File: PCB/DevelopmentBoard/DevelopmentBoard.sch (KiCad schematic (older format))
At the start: 21 parts, among them U1 Pi_CM4, U2 Barometer_Grove, U3 D24V22F5, U4 Micro-USB, U5 VN-100_Breakout, X1 XT30-F_Connector, X2 XT30-F_Connector, X3 2mmGrove_Connector

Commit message: Moved Altimeter and RF module for better I2C routing
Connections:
- wire segments 32 -> 33
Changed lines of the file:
@@
 Wire Wire Line
 	5700 6100 5700 6700
+Wire Wire Line
+	18250 2700 18250 2600
+Connection ~ 18250 2700
+Connection ~ 18250 2600
 $EndSCHEMATC

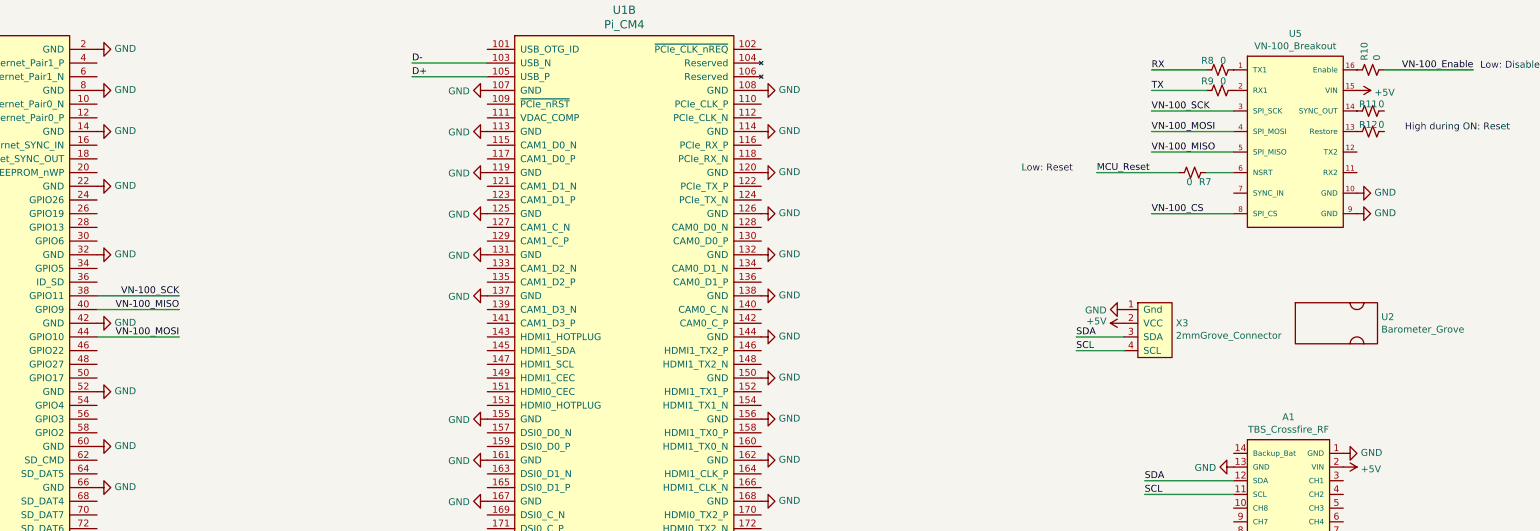
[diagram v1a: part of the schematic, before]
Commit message: Added test points
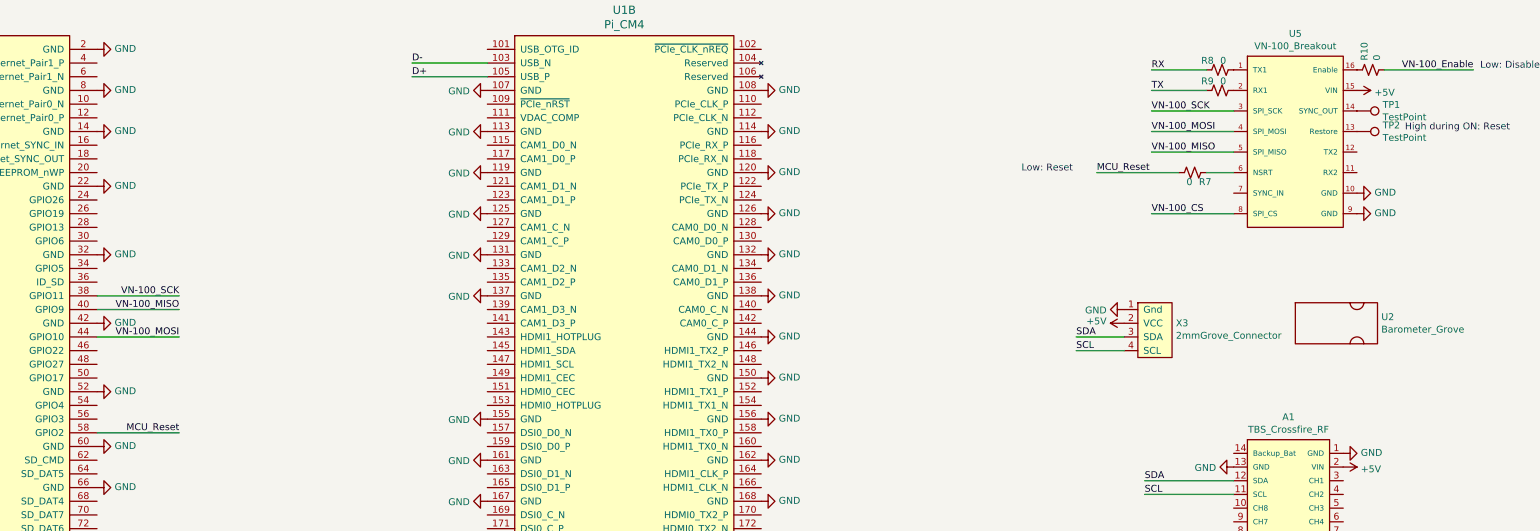
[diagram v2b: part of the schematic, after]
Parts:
- removed R11, R12: 0, PayloadFootprints:0603, symbol Device:R_Small_US
- added TP1, TP2: TestPoint, TestPoint:TestPoint_Pad_D2.0mm, symbol Connector:TestPoint
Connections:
- wire segments 33 -> 34
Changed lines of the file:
@@
 Low: Reset
-$Comp
-L Device:R_Small_US R7
-U 1 1 616A9425
-P 18550 5150
-F 0 "R7" V 18618 5196 50  0000 L CNN
-F 1 "0" V 18618 5105 50  0000 L CNN
-F 2 "PayloadFootprints:0603" H 18550 5150 50  0001 C CNN
-F 3 "~" H 18550 5150 50  0001 C CNN
-	1    18550 5150
-	0    1    1    0
-$EndComp
-Wire Wire Line
-	18650 5150 18850 5150
-Wire Wire Line
-	17850 5150 18450 5150
 $Comp
 L Device:R_Small_US R10
@@
 F 3 "~" H 19850 4400 50  0001 C CNN
 	1    19850 4400
-	0    -1   -1   0
-$EndComp
-$Comp
-L Device:R_Small_US R12
-U 1 1 616B2484
-P 19850 4850
-F 0 "R12" V 19900 4800 50  0000 L CNN
-F 1 "0" V 19900 4750 50  0000 L CNN
-F 2 "PayloadFootprints:0603" H 19850 4850 50  0001 C CNN
-F 3 "~" H 19850 4850 50  0001 C CNN
-	1    19850 4850
 	0    -1   -1   0
 $EndComp
@@
 Text Label 18250 4550 0    50   ~ 0
 TX
-$Comp
-L Device:R_Small_US R11
-U 1 1 616BF1FF
-P 19850 4700
-F 0 "R11" V 19900 4650 50  0000 L CNN
-F 1 "0" V 19900 4600 50  0000 L CNN
-F 2 "PayloadFootprints:0603" H 19850 4700 50  0001 C CNN
-F 3 "~" H 19850 4700 50  0001 C CNN
-	1    19850 4700
-	0    -1   -1   0
-$EndComp
 $Comp
 L Device:R_Small_US R9
@@
 Connection ~ 18250 2700
 Connection ~ 18250 2600
+Wire Wire Line
+	17850 5150 18450 5150
+Wire Wire Line
+	18650 5150 18850 5150
+$Comp
+L Device:R_Small_US R7
+U 1 1 616A9425
+P 18550 5150
+F 0 "R7" V 18618 5196 50  0000 L CNN
+F 1 "0" V 18618 5105 50  0000 L CNN
+F 2 "PayloadFootprints:0603" H 18550 5150 50  0001 C CNN
+F 3 "~" H 18550 5150 50  0001 C CNN
+	1    18550 5150
+	0    1    1    0
+$EndComp
+Text Label 11150 7050 2    50   ~ 0
+MCU_Reset
+Wire Wire Line
+	11150 7050 10550 7050
+$Comp
+L Connector:TestPoint TP2
+U 1 1 6167D912
+P 19750 4850
+F 0 "TP2" V 19704 5038 50  0000 L CNN
+F 1 "TestPoint" V 19795 5038 50  0000 L CNN
+F 2 "TestPoint:TestPoint_Pad_D2.0mm" H 19950 4850 50  0001 C CNN
+F 3 "~" H 19950 4850 50  0001 C CNN
+	1    19750 4850
+	0    1    1    0
+$EndComp
+$Comp
+L Connector:TestPoint TP1
+U 1 1 6167FD02
+P 19750 4700
+F 0 "TP1" V 19704 4888 50  0000 L CNN
+F 1 "TestPoint" V 19795 4888 50  0000 L CNN
+F 2 "TestPoint:TestPoint_Pad_D2.0mm" H 19950 4700 50  0001 C CNN
+F 3 "~" H 19950 4700 50  0001 C CNN
+	1    19750 4700
+	0    1    1    0
+$EndComp
 $EndSCHEMATC

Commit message: Sized traces. Moved USB connector. Uncrossed all signals.
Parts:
- removed R2, R4, R6: 0, PayloadFootprints:0603, symbol Device:R_Small_US
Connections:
- wire segments 34 -> 33
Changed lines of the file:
@@
 	1    0    0    -1
 $EndComp
-Wire Wire Line
-	6150 6100 6150 6700
 Text Label 6150 6700 1    50   ~ 0
 VN-100_CS
@@
 $EndComp
 $Comp
-L Device:R_Small_US R6
-U 1 1 6168742C
-P 6150 6000
-F 0 "R6" H 6218 6046 50  0000 L CNN
-F 1 "0" H 6218 5955 50  0000 L CNN
-F 2 "PayloadFootprints:0603" H 6150 6000 50  0001 C CNN
-F 3 "~" H 6150 6000 50  0001 C CNN
-	1    6150 6000
-	1    0    0    -1
-$EndComp
-$Comp
 L PayloadSymbols:Barometer_Grove U2
 U 1 1 6168942A
@@
 Text Label 5400 6550 3    50   ~ 0
 SDA
-$Comp
-L Device:R_Small_US R2
-U 1 1 616833BE
-P 5400 6000
-F 0 "R2" H 5468 6046 50  0000 L CNN
-F 1 "0" H 5468 5955 50  0000 L CNN
-F 2 "PayloadFootprints:0603" H 5400 6000 50  0001 C CNN
-F 3 "~" H 5400 6000 50  0001 C CNN
-	1    5400 6000
-	1    0    0    -1
-$EndComp
-$Comp
-L Device:R_Small_US R4
-U 1 1 616833C4
-P 5700 6000
-F 0 "R4" H 5768 6046 50  0000 L CNN
-F 1 "0" H 5768 5955 50  0000 L CNN
-F 2 "PayloadFootprints:0603" H 5700 6000 50  0001 C CNN
-F 3 "~" H 5700 6000 50  0001 C CNN
-	1    5700 6000
-	1    0    0    -1
-$EndComp
-Wire Wire Line
-	5400 6100 5400 6700
-Wire Wire Line
-	5700 6100 5700 6700
-Wire Wire Line
-	18250 2700 18250 2600
-Connection ~ 18250 2700
-Connection ~ 18250 2600
 Wire Wire Line
 	17850 5150 18450 5150
@@
 	0    1    1    0
 $EndComp
+Wire Wire Line
+	6150 5900 6150 6700
+Wire Wire Line
+	5700 5900 5700 6700
+Wire Wire Line
+	5400 5900 5400 6700
 $EndSCHEMATC

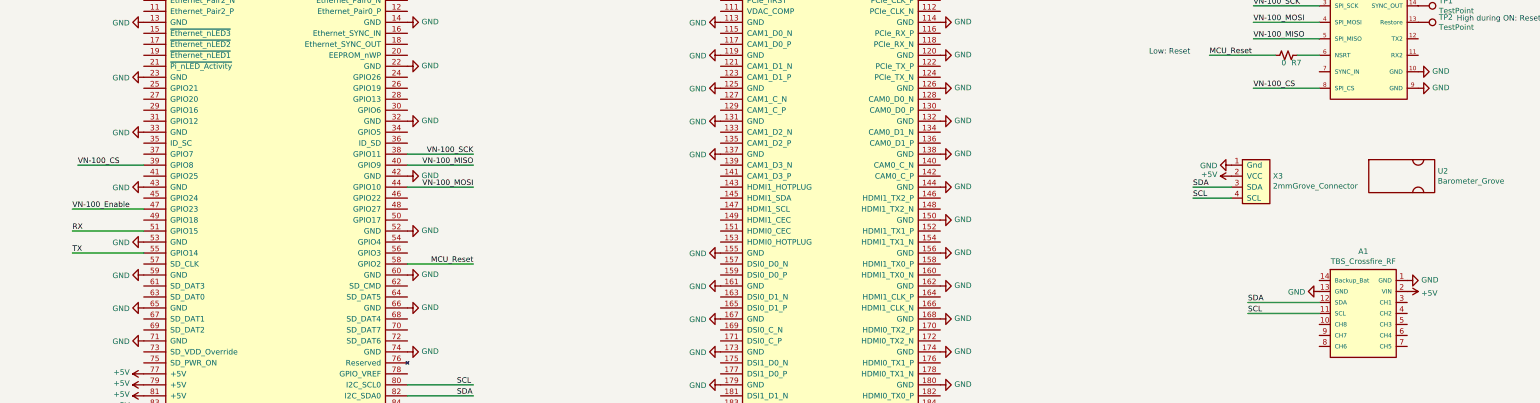
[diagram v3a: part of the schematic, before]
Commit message: step file locations changed for compatibility
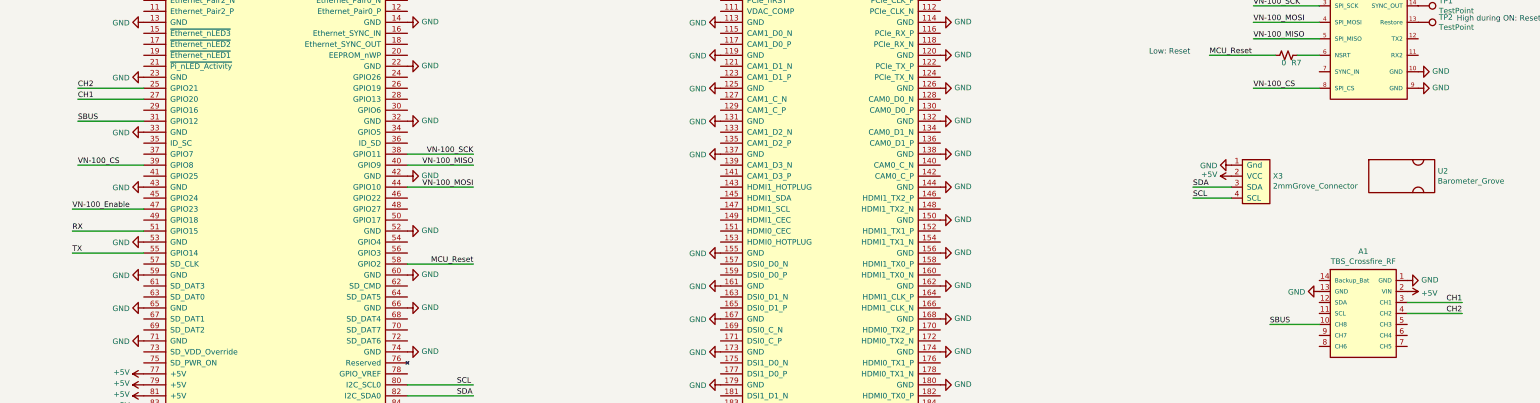
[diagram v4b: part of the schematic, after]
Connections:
- net labels added: CH1, CH2, SBUS
- wire segments 33 -> 37
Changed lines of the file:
@@
 	1    0    0    -1
 $EndComp
-Text Label 18200 7500 0    50   ~ 0
-SCL
-Text Label 18200 7400 0    50   ~ 0
-SDA
-Wire Wire Line
-	18200 7400 18850 7400
-Wire Wire Line
-	18200 7500 18850 7500
 Text Label 11000 8250 0    50   ~ 0
 SDA
@@
 Wire Wire Line
 	5400 5900 5400 6700
+Wire Wire Line
+	19650 7400 20150 7400
+Wire Wire Line
+	19650 7500 20150 7500
+Wire Wire Line
+	18850 7600 18400 7600
+Text Label 18400 7600 0    50   ~ 0
+SBUS
+Text Label 20150 7400 2    50   ~ 0
+CH1
+Text Label 20150 7500 2    50   ~ 0
+CH2
+Wire Wire Line
+	8150 5750 7550 5750
+Text Label 7550 5750 0    50   ~ 0
+SBUS
+Wire Wire Line
+	8150 5450 7550 5450
+Wire Wire Line
+	8150 5550 7550 5550
+Text Label 7550 5450 0    50   ~ 0
+CH2
+Text Label 7550 5550 0    50   ~ 0
+CH1
 $EndSCHEMATC

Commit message: adding ethernet and UART breakout shrinking width of board with necessary rearrangement
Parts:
- removed X1, X2: XT30-F_Connector, PayloadFootprints:XT30, symbol PayloadSymbols:XT30-F_Connector
- added J1: Conn_01x04_MountingPin, Connector_PinHeader_2.54mm:PinHeader_1x04_P2.54mm_Vertical, symbol PayloadSymbols:Conn_01x04_MountingPin
- added J?: RJ45_Connector_Molex_SMT_MAGwithLED, RJ45_Connector_Molex_SMT_MAGwithLED, symbol PayloadSymbols:RJ45_Connector_Molex_SMT_MAGwithLED
- added X1, X2: XT30-M_Connector, Connector_AMASS:AMASS_XT30U-M_1x02_P5.0mm_Vertical, symbol PayloadSymbols:XT30-M_Connector
- A1: footprint PayloadFootprints:TBS_Crossfire_RF -> DevelopmentBoard:TBS_Crossfire_RF
- R1, R3, R5: footprint PayloadFootprints:0603 -> DevelopmentBoard:0603
- U1: footprint PayloadFootprints:Pi_CM4 -> DevelopmentBoard:Pi_CM4
- U3: footprint PayloadFootprints:D24V22F5_VoltageRegulator -> DevelopmentBoard:D24V22F5_VoltageRegulator
- U4: footprint PayloadFootprints:GCT_USB3075-30-A -> DevelopmentBoard:GCT_USB3075-30-A
- U5: footprint PayloadFootprints:VN-100Breakout -> DevelopmentBoard:VN-100Breakout
- X3: footprint PayloadFootprints:2mmGrove_Connector -> DevelopmentBoard:2mmGrove_Connector
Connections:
- wire segments 37 -> 59
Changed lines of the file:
@@
 F 0 "U1" H 9350 4537 60  0000 C CNN
 F 1 "Pi_CM4" H 9350 4431 60  0000 C CNN
-F 2 "PayloadFootprints:Pi_CM4" H 8350 4300 60  0001 L CNN
+F 2 "DevelopmentBoard:Pi_CM4" H 8350 4300 60  0001 L CNN
 F 3 "" H 8350 4100 60  0001 L CNN
 	1    8150 4250
@@
 F 0 "U1" H 14400 4537 60  0000 C CNN
 F 1 "Pi_CM4" H 14400 4431 60  0000 C CNN
-F 2 "PayloadFootprints:Pi_CM4" H 13600 4300 60  0001 L CNN
+F 2 "DevelopmentBoard:Pi_CM4" H 13600 4300 60  0001 L CNN
 F 3 "" H 13600 4100 60  0001 L CNN
 	2    13400 4250
@@
 F 0 "U3" H 19178 2854 50  0000 L CNN
 F 1 "D24V22F5" H 19178 2763 50  0000 L CNN
-F 2 "PayloadFootprints:D24V22F5_VoltageRegulator" H 18900 2750 50  0001 C CNN
+F 2 "DevelopmentBoard:D24V22F5_VoltageRegulator" H 18900 2750 50  0001 C CNN
 F 3 "" H 18900 2750 50  0001 C CNN
 	1    18900 2750
 	1    0    0    -1
-$EndComp
-$Comp
-L PayloadSymbols:XT30-F_Connector X2
-U 1 1 61621E18
-P 18100 2650
-F 0 "X2" H 18278 2701 50  0000 L CNN
-F 1 "XT30-F_Connector" H 18278 2610 50  0000 L CNN
-F 2 "PayloadFootprints:XT30" H 18050 2650 50  0001 C CNN
-F 3 "" H 18050 2650 50  0001 C CNN
-	1    18100 2650
-	-1   0    0    1
 $EndComp
 $Comp
@@
 F 0 "R5" H 6218 5846 50  0000 L CNN
 F 1 "4.7k" H 6218 5755 50  0000 L CNN
-F 2 "PayloadFootprints:0603" H 6150 5800 50  0001 C CNN
+F 2 "DevelopmentBoard:0603" H 6150 5800 50  0001 C CNN
 F 3 "~" H 6150 5800 50  0001 C CNN
 	1    6150 5800
@@
 	18150 2300 18250 2300
 $Comp
-L PayloadSymbols:XT30-F_Connector X1
-U 1 1 6165670A
-P 18100 2250
-F 0 "X1" H 18278 2301 50  0000 L CNN
-F 1 "XT30-F_Connector" H 18278 2210 50  0000 L CNN
-F 2 "PayloadFootprints:XT30" H 18050 2250 50  0001 C CNN
-F 3 "" H 18050 2250 50  0001 C CNN
-	1    18100 2250
-	-1   0    0    1
-$EndComp
-$Comp
 L power:GND #PWR0168
 U 1 1 6161AEF3
@@
 F 0 "A1" H 19250 8065 50  0000 C CNN
 F 1 "TBS_Crossfire_RF" H 19250 7974 50  0000 C CNN
-F 2 "PayloadFootprints:TBS_Crossfire_RF" H 19250 8000 50  0001 C CNN
+F 2 "DevelopmentBoard:TBS_Crossfire_RF" H 19250 8000 50  0001 C CNN
 F 3 "" H 19250 8000 50  0001 C CNN
 	1    19250 7500
@@
 F 0 "U4" H 19328 8751 50  0000 L CNN
 F 1 "Micro-USB" H 19328 8660 50  0000 L CNN
-F 2 "PayloadFootprints:GCT_USB3075-30-A" H 19050 8750 50  0001 C CNN
+F 2 "DevelopmentBoard:GCT_USB3075-30-A" H 19050 8750 50  0001 C CNN
 F 3 "" H 19050 8750 50  0001 C CNN
 	1    19150 8700
@@
 F 0 "X3" H 18428 6351 50  0000 L CNN
 F 1 "2mmGrove_Connector" H 18428 6260 50  0000 L CNN
-F 2 "PayloadFootprints:2mmGrove_Connector" H 18300 6300 50  0001 C CNN
+F 2 "DevelopmentBoard:2mmGrove_Connector" H 18300 6300 50  0001 C CNN
 F 3 "" H 18300 6300 50  0001 C CNN
 	1    18300 6300
@@
 F 0 "U5" H 19300 5665 50  0000 C CNN
 F 1 "VN-100_Breakout" H 19300 5574 50  0000 C CNN
-F 2 "PayloadFootprints:VN-100Breakout" H 19350 5200 50  0001 C CNN
+F 2 "DevelopmentBoard:VN-100Breakout" H 19350 5200 50  0001 C CNN
 F 3 "" H 19350 5200 50  0001 C CNN
 	1    19300 4900
@@
 F 0 "R1" H 5468 5846 50  0000 L CNN
 F 1 "4.7k" H 5468 5755 50  0000 L CNN
-F 2 "PayloadFootprints:0603" H 5400 5800 50  0001 C CNN
+F 2 "DevelopmentBoard:0603" H 5400 5800 50  0001 C CNN
 F 3 "~" H 5400 5800 50  0001 C CNN
 	1    5400 5800
@@
 F 0 "R3" H 5768 5846 50  0000 L CNN
 F 1 "4.7k" H 5768 5755 50  0000 L CNN
-F 2 "PayloadFootprints:0603" H 5700 5800 50  0001 C CNN
+F 2 "DevelopmentBoard:0603" H 5700 5800 50  0001 C CNN
 F 3 "~" H 5700 5800 50  0001 C CNN
 	1    5700 5800
@@
 Text Label 7550 5550 0    50   ~ 0
 CH1
+$Comp
+L PayloadSymbols:XT30-M_Connector X1
+U 1 1 617175F8
+P 18000 2250
+F 0 "X1" H 17992 1985 50  0000 C CNN
+F 1 "XT30-M_Connector" H 17992 2076 50  0000 C CNN
+F 2 "Connector_AMASS:AMASS_XT30U-M_1x02_P5.0mm_Vertical" H 17950 2250 50  0001 C CNN
+F 3 "" H 17950 2250 50  0001 C CNN
+	1    18000 2250
+	-1   0    0    1
+$EndComp
+Wire Wire Line
+	18250 2200 18150 2200
+$Comp
+L PayloadSymbols:XT30-M_Connector X2
+U 1 1 6171A8B5
+P 18100 2650
+F 0 "X2" H 18092 2385 50  0000 C CNN
+F 1 "XT30-M_Connector" H 18092 2476 50  0000 C CNN
+F 2 "Connector_AMASS:AMASS_XT30U-M_1x02_P5.0mm_Vertical" H 18050 2650 50  0001 C CNN
+F 3 "" H 18050 2650 50  0001 C CNN
+	1    18100 2650
+	-1   0    0    1
+$EndComp
+$Comp
+L PayloadSymbols:Conn_01x04_MountingPin J1
+U 1 1 6180C683
+P 20850 5150
+F 0 "J1" H 20938 5064 50  0000 L CNN
+F 1 "Conn_01x04_MountingPin" H 20938 4973 50  0000 L CNN
+F 2 "Connector_PinHeader_2.54mm:PinHeader_1x04_P2.54mm_Vertical" H 20850 5150 50  0001 C CNN
+F 3 "~" H 20850 5150 50  0001 C CNN
+	1    20850 5150
+	1    0    0    -1
+$EndComp
+Wire Wire Line
+	19750 5000 20400 5000
+Wire Wire Line
+	20400 5000 20400 5350
+Wire Wire Line
+	20400 5350 20650 5350
+Wire Wire Line
+	19750 5150 20200 5150
+Wire Wire Line
+	20200 5150 20200 5250
+Wire Wire Line
+	20200 5250 20650 5250
+Wire Wire Line
+	20650 5050 20600 5050
+Wire Wire Line
+	20650 5150 20600 5150
+$Comp
+L power:+5V #PWR0179
+U 1 1 61815BF7
+P 20600 5150
+F 0 "#PWR0179" H 20600 5000 50  0001 C CNN
+F 1 "+5V" V 20615 5278 50  0000 L CNN
+F 2 "" H 20600 5150 50  0001 C CNN
+F 3 "" H 20600 5150 50  0001 C CNN
+	1    20600 5150
+	0    -1   -1   0
+$EndComp
+$Comp
+L power:GND #PWR0180
+U 1 1 6181C68D
+P 20600 5050
+F 0 "#PWR0180" H 20600 4800 50  0001 C CNN
+F 1 "GND" V 20605 4922 50  0000 R CNN
+F 2 "" H 20600 5050 50  0001 C CNN
+F 3 "" H 20600 5050 50  0001 C CNN
+	1    20600 5050
+	0    1    1    0
+$EndComp
+$Comp
+L PayloadSymbols:RJ45_Connector_Molex_SMT_MAGwithLED J?
+U 1 1 61762433
+P 19200 10300
+F 0 "J?" H 19200 11317 50  0000 C CNN
+F 1 "RJ45_Connector_Molex_SMT_MAGwithLED" H 19200 11226 50  0000 C CNN
+F 2 "RJ45_Connector_Molex_SMT_MAGwithLED" H 19200 11225 50  0001 C CNN
+F 3 "https://abracon.com/Magnetics/lan/ARJP11A.PDF" H 19050 10225 50  0001 C CNN
+	1    19200 10300
+	1    0    0    -1
+$EndComp
+Wire Wire Line
+	10550 4350 11000 4350
+Wire Wire Line
+	10550 4450 11000 4450
+Wire Wire Line
+	8150 4350 7650 4350
+Wire Wire Line
+	8150 4450 7650 4450
+Wire Wire Line
+	10550 4650 11000 4650
+Wire Wire Line
+	10550 4750 11000 4750
+Wire Wire Line
+	10550 4950 11000 4950
+Wire Wire Line
+	10550 5050 11000 5050
+Wire Wire Line
+	8150 5150 7650 5150
+Wire Wire Line
+	8150 5050 7650 5050
+Wire Wire Line
+	8150 4950 7650 4950
+Wire Wire Line
+	8150 4750 7650 4750
+Wire Wire Line
+	8150 4650 7650 4650
+$Comp
+L power:GND #PWR?
+U 1 1 6178AD00
+P 19900 11400
+F 0 "#PWR?" H 19900 11150 50  0001 C CNN
+F 1 "GND" H 19905 11227 50  0000 C CNN
+F 2 "" H 19900 11400 50  0001 C CNN
+F 3 "" H 19900 11400 50  0001 C CNN
+	1    19900 11400
+	1    0    0    -1
+$EndComp
 $EndSCHEMATC

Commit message: giving up on ethernet for now, added a couple of open source breakout designs for reference
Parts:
- removed J?: RJ45_Connector_Molex_SMT_MAGwithLED, RJ45_Connector_Molex_SMT_MAGwithLED, symbol PayloadSymbols:RJ45_Connector_Molex_SMT_MAGwithLED
- added D1: LED, DevelopmentBoard:Indicator-LED, symbol Device:LED
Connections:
- net labels added: ETH_LED_1, ETH_LED_2, ETH_P0_N, ETH_P0_P, ETH_P1_N, ETH_P1_P, ETH_P2_N, ETH_P2_P, ETH_P3_N, ETH_P3_P
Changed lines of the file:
@@
 	0    1    1    0
-$EndComp
-$Comp
-L PayloadSymbols:RJ45_Connector_Molex_SMT_MAGwithLED J?
-U 1 1 61762433
-P 19200 10300
-F 0 "J?" H 19200 11317 50  0000 C CNN
-F 1 "RJ45_Connector_Molex_SMT_MAGwithLED" H 19200 11226 50  0000 C CNN
-F 2 "RJ45_Connector_Molex_SMT_MAGwithLED" H 19200 11225 50  0001 C CNN
-F 3 "https://abracon.com/Magnetics/lan/ARJP11A.PDF" H 19050 10225 50  0001 C CNN
-	1    19200 10300
-	1    0    0    -1
 $EndComp
 Wire Wire Line
@@
 	8150 5050 7650 5050
 Wire Wire Line
-	8150 4950 7650 4950
-Wire Wire Line
 	8150 4750 7650 4750
 Wire Wire Line
 	8150 4650 7650 4650
+Text Label 7650 5150 0    50   ~ 0
+ETH_LED_1
+Text Label 7650 5050 0    50   ~ 0
+ETH_LED_2
+Text Label 7650 4650 0    50   ~ 0
+ETH_P2_N
+Text Label 7650 4750 0    50   ~ 0
+ETH_P2_P
+Text Label 7650 4350 0    50   ~ 0
+ETH_P3_P
+Text Label 7650 4450 0    50   ~ 0
+ETH_P3_N
+Text Label 11000 4450 2    50   ~ 0
+ETH_P1_N
+Text Label 11000 4350 2    50   ~ 0
+ETH_P1_P
+Text Label 11000 4650 2    50   ~ 0
+ETH_P0_N
+Text Label 11000 4750 2    50   ~ 0
+ETH_P0_P
 $Comp
-L power:GND #PWR?
-U 1 1 6178AD00
-P 19900 11400
-F 0 "#PWR?" H 19900 11150 50  0001 C CNN
-F 1 "GND" H 19905 11227 50  0000 C CNN
-F 2 "" H 19900 11400 50  0001 C CNN
-F 3 "" H 19900 11400 50  0001 C CNN
-	1    19900 11400
+L Device:LED D1
+U 1 1 6179A582
+P 7850 8950
+F 0 "D1" H 7843 9167 50  0000 C CNN
+F 1 "LED" H 7843 9076 50  0000 C CNN
+F 2 "DevelopmentBoard:Indicator-LED" H 7850 8950 50  0001 C CNN
+F 3 "~" H 7850 8950 50  0001 C CNN
+	1    7850 8950
 	1    0    0    -1
 $EndComp
+$Comp
+L power:GND #PWR0182
+U 1 1 6179C96B
+P 7700 8950
+F 0 "#PWR0182" H 7700 8700 50  0001 C CNN
+F 1 "GND" H 7705 8777 50  0000 C CNN
+F 2 "" H 7700 8950 50  0001 C CNN
+F 3 "" H 7700 8950 50  0001 C CNN
+	1    7700 8950
+	-1   0    0    1
+$EndComp
+Wire Wire Line
+	8150 8950 8000 8950
 $EndSCHEMATC
